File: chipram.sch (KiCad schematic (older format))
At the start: 26 parts, among them J500 Jumper_2_Bridged, U500 62402, U501 XX4256-15, U502 XX4256-15, U503 XX4256-15, U504 XX4256-15, U505 XX4256-15, U506 XX4256-15, U507 XX4256-15, U508 XX4256-15, U540 74F244, U541 74F244

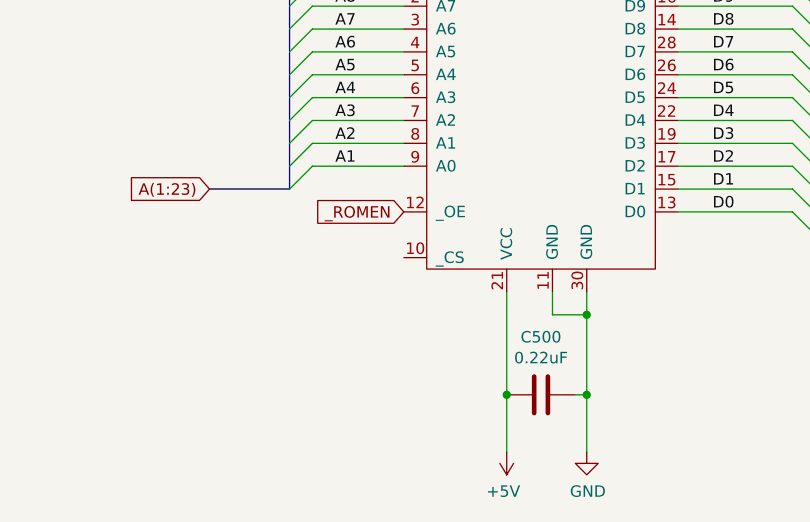
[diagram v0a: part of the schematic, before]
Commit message: Fix some DRC fuckery
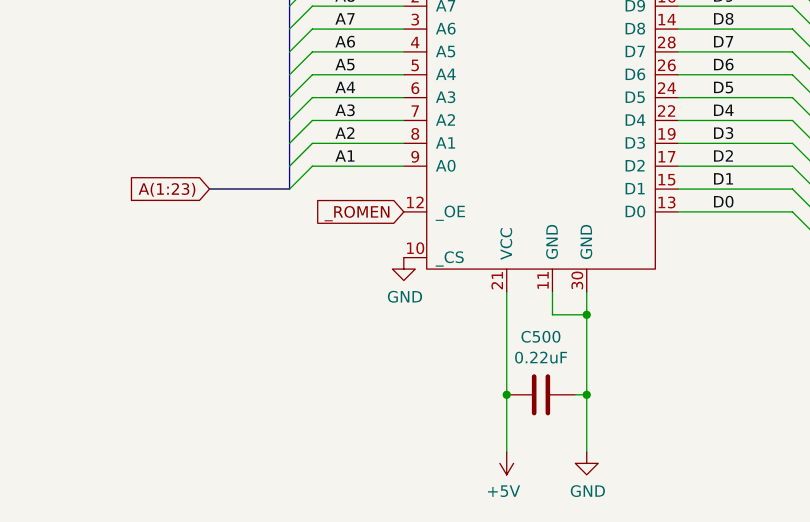
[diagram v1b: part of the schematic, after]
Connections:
- net GND: now also U500.10 (_CS)
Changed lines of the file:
@@
 Wire Bus Line
 	7350 9800 15750 9800
+$Comp
+L power:GND #PWR0257
+U 1 1 7152E7BF
+P 2500 10100
+F 0 "#PWR0257" H 2500 9850 50  0001 C CNN
+F 1 "GND" H 2505 9927 50  0000 C CNN
+F 2 "" H 2500 10100 50  0001 C CNN
+F 3 "" H 2500 10100 50  0001 C CNN
+	1    2500 10100
+	1    0    0    -1
+$EndComp
 $EndSCHEMATC

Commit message: drc
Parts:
- added C540, C541: 0.1uF, symbol Device:C
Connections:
- net +5V: now also U540.20 (VCC), U541.20 (VCC), C540.2, C541.2
- net GND: now also U540.1 (OEa), U540.10 (GND), U540.19 (OEb), U541.1 (OEa), U541.10 (GND), U541.19 (OEb), C540.1, C541.1
- net at RP502.1 (R1.1), U501.4 (_RAS), U502.4 (_RAS)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: no longer U505.4 (_RAS), U506.4 (_RAS), U507.4 (_RAS), U508.4 (_RAS)
- net at RP502.5 (R3.1): now also U505.4 (_RAS), U506.4 (_RAS), U507.4 (_RAS), U508.4 (_RAS)
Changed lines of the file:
@@
 	3650 3750 3650 5000
-Wire Wire Line
-	3650 5000 6300 5000
 Wire Wire Line
 	7200 5000 9700 5000
@@
 Connection ~ 12200 5000
 Wire Wire Line
-	6300 5000 6300 8000
-Wire Wire Line
-	6300 8000 7200 8000
-Connection ~ 6300 5000
-Wire Wire Line
-	6300 5000 7200 5000
-Wire Wire Line
 	7200 8000 9700 8000
-Connection ~ 7200 8000
 Wire Wire Line
 	9700 8000 12150 8000
@@
 Text GLabel 7350 9800 0    50   Input ~ 0
 DRD(0:15)
-Wire Bus Line
-	3750 1850 5850 1850
-Wire Bus Line
-	3750 3250 5850 3250
-Wire Bus Line
-	5850 1850 5850 3250
-Wire Bus Line
-	1250 1200 1250 3150
-Wire Bus Line
-	4300 8500 4300 10000
-Wire Bus Line
-	11750 3900 11750 9100
-Wire Bus Line
-	2000 8100 2000 9800
-Wire Bus Line
-	13800 3900 13800 9100
-Wire Bus Line
-	9300 3900 9300 9100
-Wire Bus Line
-	6800 3900 6800 9100
-Wire Bus Line
-	7650 6800 15750 6800
-Wire Bus Line
-	7350 9800 15750 9800
 $Comp
 L power:GND #PWR0257
@@
 	1    0    0    -1
 $EndComp
+Wire Wire Line
+	1600 2300 700  2300
+Wire Wire Line
+	700  2300 700  2400
+Wire Wire Line
+	700  2400 1600 2400
+Wire Wire Line
+	700  2400 700  2700
+Wire Wire Line
+	700  4150 1600 4150
+Connection ~ 700  2400
+Wire Wire Line
+	1600 4250 700  4250
+Wire Wire Line
+	700  4250 700  4150
+Connection ~ 700  4150
+$Comp
+L power:GND #PWR0258
+U 1 1 715AAAF3
+P 700 4650
+F 0 "#PWR0258" H 700 4400 50  0001 C CNN
+F 1 "GND" H 705 4477 50  0000 C CNN
+F 2 "" H 700 4650 50  0001 C CNN
+F 3 "" H 700 4650 50  0001 C CNN
+	1    700  4650
+	1    0    0    -1
+$EndComp
+Wire Wire Line
+	700  4250 700  4550
+Connection ~ 700  4250
+Wire Wire Line
+	2100 4550 700  4550
+Connection ~ 700  4550
+Wire Wire Line
+	700  4550 700  4650
+Wire Wire Line
+	2100 2700 700  2700
+Connection ~ 700  2700
+Wire Wire Line
+	700  2700 700  4150
+$Comp
+L Device:C C540
+U 1 1 716271D2
+P 2450 850
+F 0 "C540" H 2565 896 50  0000 L CNN
+F 1 "0.1uF" H 2565 805 50  0000 L CNN
+F 2 "" H 2488 700 50  0001 C CNN
+F 3 "~" H 2450 850 50  0001 C CNN
+	1    2450 850
+	1    0    0    -1
+$EndComp
+$Comp
+L Device:C C541
+U 1 1 71627735
+P 2500 2800
+F 0 "C541" H 2615 2846 50  0000 L CNN
+F 1 "0.1uF" H 2615 2755 50  0000 L CNN
+F 2 "" H 2538 2650 50  0001 C CNN
+F 3 "~" H 2500 2800 50  0001 C CNN
+	1    2500 2800
+	1    0    0    -1
+$EndComp
+Wire Wire Line
+	2250 2700 2250 2650
+Wire Wire Line
+	2250 2650 2500 2650
+Wire Wire Line
+	2100 2700 2250 2700
+Connection ~ 2100 2700
+Wire Wire Line
+	2500 2950 2100 2950
+$Comp
+L power:+5V #PWR0259
+U 1 1 716A9775
+P 1950 2900
+F 0 "#PWR0259" H 1950 2750 50  0001 C CNN
+F 1 "+5V" V 1965 3028 50  0000 L CNN
+F 2 "" H 1950 2900 50  0001 C CNN
+F 3 "" H 1950 2900 50  0001 C CNN
+	1    1950 2900
+	0    -1   -1   0
+$EndComp
+Connection ~ 2100 2950
+Wire Wire Line
+	1950 2900 2100 2900
+Wire Wire Line
+	2100 2900 2100 2950
+$Comp
+L power:+5V #PWR0260
+U 1 1 716D557D
+P 1950 1050
+F 0 "#PWR0260" H 1950 900 50  0001 C CNN
+F 1 "+5V" V 1965 1178 50  0000 L CNN
+F 2 "" H 1950 1050 50  0001 C CNN
+F 3 "" H 1950 1050 50  0001 C CNN
+	1    1950 1050
+	0    -1   -1   0
+$EndComp
+Wire Wire Line
+	1950 1050 2100 1050
+Wire Wire Line
+	2100 1050 2100 1100
+Wire Wire Line
+	2100 1050 2450 1050
+Wire Wire Line
+	2450 1050 2450 1000
+Connection ~ 2100 1050
+Wire Wire Line
+	700  700  2450 700
+Wire Wire Line
+	700  700  700  2300
+Connection ~ 700  2300
+Wire Wire Line
+	3650 5000 7200 5000
+Wire Wire Line
+	4250 8000 7200 8000
+Wire Wire Line
+	4250 3750 4250 8000
+Wire Bus Line
+	3750 1850 5850 1850
+Wire Bus Line
+	3750 3250 5850 3250
+Wire Bus Line
+	5850 1850 5850 3250
+Wire Bus Line
+	1250 1200 1250 3150
+Wire Bus Line
+	4300 8500 4300 10000
+Wire Bus Line
+	11750 3900 11750 9100
+Wire Bus Line
+	2000 8100 2000 9800
+Wire Bus Line
+	13800 3900 13800 9100
+Wire Bus Line
+	9300 3900 9300 9100
+Wire Bus Line
+	6800 3900 6800 9100
+Wire Bus Line
+	7650 6800 15750 6800
+Wire Bus Line
+	7350 9800 15750 9800
+Connection ~ 7200 8000
 $EndSCHEMATC

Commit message: Rename bus with correct syntax
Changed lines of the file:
@@
-EESchema Schematic File Version 4
+EESchema Schematic File Version 5
 LIBS:amiga2000-cache
 EELAYER 29 0
@@
 	4800 10000 4300 10000
 Text GLabel 1650 9800 0    50   Input ~ 0
-A(1:23)
+A[1..23]
 Text GLabel 4800 10000 2    50   Input ~ 0
-D(0:15)
+D[0..15]
 Text Label 2200 8000 0    50   ~ 0
 A18
@@
 	1250 2000 1350 2100
 Text GLabel 950  1200 0    50   Input ~ 0
-DRA(0:8)
+DRA[0..8]
 Wire Bus Line
 	950  1200 1250 1200
@@
 	15750 6800 15750 9800
 Text GLabel 7350 9800 0    50   Input ~ 0
-DRD(0:15)
+DRD[0..15]
 $Comp
 L power:GND #PWR0257
@@
 Wire Wire Line
 	4250 3750 4250 8000
+Connection ~ 7200 8000
 Wire Bus Line
 	3750 1850 5850 1850
@@
 Wire Bus Line
 	7350 9800 15750 9800
-Connection ~ 7200 8000
 $EndSCHEMATC

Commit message: Some ERC things
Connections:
- net +5V: now also C503.2, U503.10 (VCC); no longer C503.1, U503.20 (GND)
- net GND: now also C503.1, U503.20 (GND); no longer C503.2, U503.10 (VCC)
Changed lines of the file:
@@
-EESchema Schematic File Version 5
+EESchema Schematic File Version 4
 LIBS:amiga2000-cache
 EELAYER 29 0
@@
 L power:GND #PWR091
 U 1 1 5E8BEEE2
+P 13050 4300
+F 0 "#PWR091" H 13050 4050 50  0001 C CNN
+F 1 "GND" V 13055 4172 50  0000 R CNN
+F 2 "" H 13050 4300 50  0001 C CNN
+F 3 "" H 13050 4300 50  0001 C CNN
+	1    13050 4300
+	0    -1   -1   0
+$EndComp
+$Comp
+L power:+5V #PWR093
+U 1 1 5E8BEEE8
 P 12550 4300
-F 0 "#PWR091" H 12550 4050 50  0001 C CNN
-F 1 "GND" V 12555 4172 50  0000 R CNN
+F 0 "#PWR093" H 12550 4150 50  0001 C CNN
+F 1 "+5V" V 12565 4428 50  0000 L CNN
 F 2 "" H 12550 4300 50  0001 C CNN
 F 3 "" H 12550 4300 50  0001 C CNN
 	1    12550 4300
-	0    1    1    0
-$EndComp
-$Comp
-L power:+5V #PWR093
-U 1 1 5E8BEEE8
-P 13050 4300
-F 0 "#PWR093" H 13050 4150 50  0001 C CNN
-F 1 "+5V" V 13065 4428 50  0000 L CNN
-F 2 "" H 13050 4300 50  0001 C CNN
-F 3 "" H 13050 4300 50  0001 C CNN
-	1    13050 4300
-	0    1    1    0
-$EndComp
-Wire Wire Line
+	0    -1   -1   0
+$EndComp
+Wire Wire Line

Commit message: squeak
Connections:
- net +5V: now also C501.2, C502.2, C504.2, C505.2, C506.2, C507.2, C508.2, U501.10 (VCC), U502.10 (VCC), U504.10 (VCC), U505.10 (VCC), U506.10 (VCC), U507.10 (VCC), U508.10 (VCC); no longer C501.1, C502.1, C504.1, C505.1, C506.1, C507.1, C508.1, U501.20 (GND), U502.20 (GND), U504.20 (GND), U505.20 (GND), U506.20 (GND), U507.20 (GND), U508.20 (GND)
- net GND: now also C501.1, C502.1, C504.1, C505.1, C506.1, C507.1, C508.1, U501.20 (GND), U502.20 (GND), U504.20 (GND), U505.20 (GND), U506.20 (GND), U507.20 (GND), U508.20 (GND); no longer C501.2, C502.2, C504.2, C505.2, C506.2, C507.2, C508.2, U501.10 (VCC), U502.10 (VCC), U504.10 (VCC), U505.10 (VCC), U506.10 (VCC), U507.10 (VCC), U508.10 (VCC)
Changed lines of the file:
@@
 L power:GND #PWR078
 U 1 1 5E8B4169
+P 8050 4300
+F 0 "#PWR078" H 8050 4050 50  0001 C CNN
+F 1 "GND" V 8055 4172 50  0000 R CNN
+F 2 "" H 8050 4300 50  0001 C CNN
+F 3 "" H 8050 4300 50  0001 C CNN
+	1    8050 4300
+	0    -1   -1   0
+$EndComp
+$Comp
+L power:+5V #PWR080
+U 1 1 5E8B4981
 P 7550 4300
-F 0 "#PWR078" H 7550 4050 50  0001 C CNN
-F 1 "GND" V 7555 4172 50  0000 R CNN
+F 0 "#PWR080" H 7550 4150 50  0001 C CNN
+F 1 "+5V" V 7565 4428 50  0000 L CNN
 F 2 "" H 7550 4300 50  0001 C CNN
 F 3 "" H 7550 4300 50  0001 C CNN
 	1    7550 4300
-	0    1    1    0
-$EndComp
-$Comp
-L power:+5V #PWR080
-U 1 1 5E8B4981
-P 8050 4300
-F 0 "#PWR080" H 8050 4150 50  0001 C CNN
-F 1 "+5V" V 8065 4428 50  0000 L CNN
-F 2 "" H 8050 4300 50  0001 C CNN
-F 3 "" H 8050 4300 50  0001 C CNN
-	1    8050 4300
-	0    1    1    0
+	0    -1   -1   0
 $EndComp
 Wire Wire Line
@@
 L power:GND #PWR084
 U 1 1 5E8BAB5E
+P 10550 4300
+F 0 "#PWR084" H 10550 4050 50  0001 C CNN
+F 1 "GND" V 10555 4172 50  0000 R CNN
+F 2 "" H 10550 4300 50  0001 C CNN
+F 3 "" H 10550 4300 50  0001 C CNN
+	1    10550 4300
+	0    -1   -1   0
+$EndComp
+$Comp
+L power:+5V #PWR086
+U 1 1 5E8BAB68
 P 10050 4300
-F 0 "#PWR084" H 10050 4050 50  0001 C CNN
-F 1 "GND" V 10055 4172 50  0000 R CNN
+F 0 "#PWR086" H 10050 4150 50  0001 C CNN
+F 1 "+5V" V 10065 4428 50  0000 L CNN
 F 2 "" H 10050 4300 50  0001 C CNN
 F 3 "" H 10050 4300 50  0001 C CNN
 	1    10050 4300
-	0    1    1    0
-$EndComp
-$Comp
-L power:+5V #PWR086
-U 1 1 5E8BAB68
-P 10550 4300
-F 0 "#PWR086" H 10550 4150 50  0001 C CNN
-F 1 "+5V" V 10565 4428 50  0000 L CNN
-F 2 "" H 10550 4300 50  0001 C CNN
-F 3 "" H 10550 4300 50  0001 C CNN
-	1    10550 4300
-	0    1    1    0
+	0    -1   -1   0
 $EndComp
 Wire Wire Line
@@
 L power:GND #PWR096
 U 1 1 5E8C19D1
+P 15050 4300
+F 0 "#PWR096" H 15050 4050 50  0001 C CNN
+F 1 "GND" V 15055 4172 50  0000 R CNN
+F 2 "" H 15050 4300 50  0001 C CNN
+F 3 "" H 15050 4300 50  0001 C CNN
+	1    15050 4300
+	0    -1   -1   0
+$EndComp
+$Comp
+L power:+5V #PWR098
+U 1 1 5E8C19D7
 P 14550 4300
-F 0 "#PWR096" H 14550 4050 50  0001 C CNN
-F 1 "GND" V 14555 4172 50  0000 R CNN
+F 0 "#PWR098" H 14550 4150 50  0001 C CNN
+F 1 "+5V" V 14565 4428 50  0000 L CNN
 F 2 "" H 14550 4300 50  0001 C CNN
 F 3 "" H 14550 4300 50  0001 C CNN
 	1    14550 4300
-	0    1    1    0
-$EndComp
-$Comp
-L power:+5V #PWR098
-U 1 1 5E8C19D7
-P 15050 4300
-F 0 "#PWR098" H 15050 4150 50  0001 C CNN
-F 1 "+5V" V 15065 4428 50  0000 L CNN
-F 2 "" H 15050 4300 50  0001 C CNN
-F 3 "" H 15050 4300 50  0001 C CNN
-	1    15050 4300
-	0    1    1    0
+	0    -1   -1   0
 $EndComp
 Wire Wire Line
@@
 L power:GND #PWR097
 U 1 1 5E8C4677
+P 15050 7300
+F 0 "#PWR097" H 15050 7050 50  0001 C CNN
+F 1 "GND" V 15055 7172 50  0000 R CNN
+F 2 "" H 15050 7300 50  0001 C CNN
+F 3 "" H 15050 7300 50  0001 C CNN
+	1    15050 7300
+	0    -1   -1   0
+$EndComp
+$Comp
+L power:+5V #PWR099
+U 1 1 5E8C467D
 P 14550 7300
-F 0 "#PWR097" H 14550 7050 50  0001 C CNN
-F 1 "GND" V 14555 7172 50  0000 R CNN
+F 0 "#PWR099" H 14550 7150 50  0001 C CNN
+F 1 "+5V" V 14565 7428 50  0000 L CNN
 F 2 "" H 14550 7300 50  0001 C CNN
 F 3 "" H 14550 7300 50  0001 C CNN
 	1    14550 7300
-	0    1    1    0
-$EndComp
-$Comp
-L power:+5V #PWR099
-U 1 1 5E8C467D
-P 15050 7300
-F 0 "#PWR099" H 15050 7150 50  0001 C CNN
-F 1 "+5V" V 15065 7428 50  0000 L CNN
-F 2 "" H 15050 7300 50  0001 C CNN
-F 3 "" H 15050 7300 50  0001 C CNN
-	1    15050 7300
-	0    1    1    0
+	0    -1   -1   0
 $EndComp
 Wire Wire Line
@@
 L power:GND #PWR090
 U 1 1 5E8CAD29
+P 13000 7300
+F 0 "#PWR090" H 13000 7050 50  0001 C CNN
+F 1 "GND" V 13005 7172 50  0000 R CNN
+F 2 "" H 13000 7300 50  0001 C CNN
+F 3 "" H 13000 7300 50  0001 C CNN
+	1    13000 7300
+	0    -1   -1   0
+$EndComp
+$Comp
+L power:+5V #PWR092
+U 1 1 5E8CAD2F
 P 12500 7300
-F 0 "#PWR090" H 12500 7050 50  0001 C CNN
-F 1 "GND" V 12505 7172 50  0000 R CNN
+F 0 "#PWR092" H 12500 7150 50  0001 C CNN
+F 1 "+5V" V 12515 7428 50  0000 L CNN
 F 2 "" H 12500 7300 50  0001 C CNN
 F 3 "" H 12500 7300 50  0001 C CNN
 	1    12500 7300
-	0    1    1    0
-$EndComp
-$Comp
-L power:+5V #PWR092
-U 1 1 5E8CAD2F
-P 13000 7300
-F 0 "#PWR092" H 13000 7150 50  0001 C CNN
-F 1 "+5V" V 13015 7428 50  0000 L CNN
-F 2 "" H 13000 7300 50  0001 C CNN
-F 3 "" H 13000 7300 50  0001 C CNN
-	1    13000 7300
-	0    1    1    0
-$EndComp
-Wire Wire Line
-	13000 7300 12950 7300
-Wire Wire Line
-	12500 7300 12550 7300
-Wire Wire Line
-	12550 7300 12550 7450
-Wire Wire Line
-	12700 7450 12700 7600
-Wire Wire Line
-	12550 7450 12700 7450
-Connection ~ 12550 7300
-Wire Wire Line
-	12550 7300 12600 7300
-Wire Wire Line
-	12800 7450 12950 7450
-Wire Wire Line
-	12950 7450 12950 7300
-Connection ~ 12950 7300
-Wire Wire Line
-	12950 7300 12900 7300
+	0    -1   -1   0
+$EndComp
 Wire Wire Line
 	12800 7450 12800 7600
@@
 L power:GND #PWR085
 U 1 1 5E8D123B
+P 10550 7300
+F 0 "#PWR085" H 10550 7050 50  0001 C CNN
+F 1 "GND" V 10555 7172 50  0000 R CNN
+F 2 "" H 10550 7300 50  0001 C CNN
+F 3 "" H 10550 7300 50  0001 C CNN
+	1    10550 7300
+	0    -1   -1   0
+$EndComp
+$Comp
+L power:+5V #PWR087
+U 1 1 5E8D1241
 P 10050 7300
-F 0 "#PWR085" H 10050 7050 50  0001 C CNN
-F 1 "GND" V 10055 7172 50  0000 R CNN
+F 0 "#PWR087" H 10050 7150 50  0001 C CNN
+F 1 "+5V" V 10065 7428 50  0000 L CNN
 F 2 "" H 10050 7300 50  0001 C CNN
 F 3 "" H 10050 7300 50  0001 C CNN
 	1    10050 7300
-	0    1    1    0
-$EndComp
-$Comp
-L power:+5V #PWR087
-U 1 1 5E8D1241
-P 10550 7300
-F 0 "#PWR087" H 10550 7150 50  0001 C CNN
-F 1 "+5V" V 10565 7428 50  0000 L CNN
-F 2 "" H 10550 7300 50  0001 C CNN
-F 3 "" H 10550 7300 50  0001 C CNN
-	1    10550 7300
-	0    1    1    0
+	0    -1   -1   0
 $EndComp
 Wire Wire Line
@@
 L power:GND #PWR079
 U 1 1 5E8D49C4
+P 8050 7300
+F 0 "#PWR079" H 8050 7050 50  0001 C CNN
+F 1 "GND" V 8055 7172 50  0000 R CNN
+F 2 "" H 8050 7300 50  0001 C CNN
+F 3 "" H 8050 7300 50  0001 C CNN
+	1    8050 7300
+	0    -1   -1   0
+$EndComp
+$Comp
+L power:+5V #PWR081
+U 1 1 5E8D49CA
 P 7550 7300
-F 0 "#PWR079" H 7550 7050 50  0001 C CNN
-F 1 "GND" V 7555 7172 50  0000 R CNN
+F 0 "#PWR081" H 7550 7150 50  0001 C CNN
+F 1 "+5V" V 7565 7428 50  0000 L CNN
 F 2 "" H 7550 7300 50  0001 C CNN
 F 3 "" H 7550 7300 50  0001 C CNN
 	1    7550 7300
-	0    1    1    0
-$EndComp
-$Comp
-L power:+5V #PWR081
-U 1 1 5E8D49CA
-P 8050 7300
-F 0 "#PWR081" H 8050 7150 50  0001 C CNN
-F 1 "+5V" V 8065 7428 50  0000 L CNN
-F 2 "" H 8050 7300 50  0001 C CNN
-F 3 "" H 8050 7300 50  0001 C CNN
-	1    8050 7300
-	0    1    1    0
+	0    -1   -1   0
 $EndComp
 Wire Wire Line
@@
 L power:GND #PWR0257
 U 1 1 7152E7BF
-P 2500 10100
-F 0 "#PWR0257" H 2500 9850 50  0001 C CNN
-F 1 "GND" H 2505 9927 50  0000 C CNN
-F 2 "" H 2500 10100 50  0001 C CNN
-F 3 "" H 2500 10100 50  0001 C CNN
-	1    2500 10100
+P 2400 10250
+F 0 "#PWR0257" H 2400 10000 50  0001 C CNN
+F 1 "GND" H 2405 10077 50  0000 C CNN
+F 2 "" H 2400 10250 50  0001 C CNN
+F 3 "" H 2400 10250 50  0001 C CNN
+	1    2400 10250
 	1    0    0    -1
 $EndComp
@@
 	4250 3750 4250 8000
 Connection ~ 7200 8000
+Wire Wire Line
+	2400 10250 2400 10100
+Wire Wire Line
+	2400 10100 2500 10100
+Wire Wire Line
+	12800 7450 12950 7450
+Wire Wire Line
+	12950 7450 12950 7300
+Wire Wire Line
+	12950 7300 12900 7300
+Wire Wire Line
+	12950 7300 13000 7300
+Connection ~ 12950 7300
+Wire Wire Line
+	12700 7600 12700 7450
+Wire Wire Line
+	12700 7450 12550 7450
+Wire Wire Line
+	12550 7450 12550 7300
+Wire Wire Line
+	12550 7300 12600 7300
+Wire Wire Line
+	12550 7300 12500 7300
 Wire Bus Line
 	3750 1850 5850 1850
@@
 Wire Bus Line
 	7350 9800 15750 9800
+Connection ~ 12550 7300
 $EndSCHEMATC

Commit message: Associate footprints with components
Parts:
- J500: footprint (none) -> Connector_PinSocket_2.54mm:PinSocket_2x01_P2.54mm_Vertical
- R500: footprint (none) -> Resistor_THT:R_Axial_DIN0207_L6.3mm_D2.5mm_P10.16mm_Horizontal
- U500: footprint (none) -> Package_DIP:DIP-40_W15.24mm_Socket
- U501, U502, U503, U504, U505, U506, U507, U508, U540, U541: footprint (none) -> Package_DIP:DIP-20_W7.62mm_Socket
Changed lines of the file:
@@
 F 0 "U540" H 2250 2600 50  0000 C CNN
 F 1 "74F244" H 1850 2600 50  0000 C CNN
-F 2 "" H 2100 1900 50  0001 C CNN
+F 2 "Package_DIP:DIP-20_W7.62mm_Socket" H 2100 1900 50  0001 C CNN
 F 3 "http://www.ti.com/lit/gpn/sn74LS244" H 2100 1900 50  0001 C CNN
 	1    2100 1900
@@
 F 0 "U541" H 2250 4450 50  0000 C CNN
 F 1 "74F244" H 1850 4450 50  0000 C CNN
-F 2 "" H 2100 3750 50  0001 C CNN
+F 2 "Package_DIP:DIP-20_W7.62mm_Socket" H 2100 3750 50  0001 C CNN
 F 3 "http://www.ti.com/lit/gpn/sn74LS244" H 2100 3750 50  0001 C CNN
 	1    2100 3750
@@
 F 0 "U500" H 3100 8025 50  0000 C CNN
 F 1 "62402" H 3100 7934 50  0000 C CNN
-F 2 "" H 3100 7900 50  0001 C CNN
+F 2 "Package_DIP:DIP-40_W15.24mm_Socket" H 3100 7900 50  0001 C CNN
 F 3 "" H 3100 7900 50  0001 C CNN
 	1    3100 7900
@@
 F 0 "R500" H 1370 7296 50  0000 L CNN
 F 1 "4.7k" H 1370 7205 50  0000 L CNN
-F 2 "" V 1230 7250 50  0001 C CNN
+F 2 "Resistor_THT:R_Axial_DIN0207_L6.3mm_D2.5mm_P10.16mm_Horizontal" V 1230 7250 50  0001 C CNN
 F 3 "~" H 1300 7250 50  0001 C CNN
 	1    1300 7250
@@
 F 0 "J500" H 1750 7603 50  0000 C CNN
 F 1 "Jumper_2_Bridged" H 1750 7604 50  0001 C CNN
-F 2 "" H 1750 7500 50  0001 C CNN
+F 2 "Connector_PinSocket_2.54mm:PinSocket_2x01_P2.54mm_Vertical" H 1750 7500 50  0001 C CNN
 F 3 "~" H 1750 7500 50  0001 C CNN
 	1    1750 7500
@@
 F 0 "U501" H 8078 3971 50  0000 L CNN
 F 1 "XX4256-15" H 8078 3880 50  0000 L CNN
-F 2 "" H 7700 4700 50  0001 C CNN
+F 2 "Package_DIP:DIP-20_W7.62mm_Socket" H 7700 4700 50  0001 C CNN
 F 3 "" H 7700 4700 50  0001 C CNN
 	1    7700 4700
@@
 F 0 "U505" H 8078 6971 50  0000 L CNN
 F 1 "XX4256-15" H 8078 6880 50  0000 L CNN
-F 2 "" H 7700 7700 50  0001 C CNN
+F 2 "Package_DIP:DIP-20_W7.62mm_Socket" H 7700 7700 50  0001 C CNN
 F 3 "" H 7700 7700 50  0001 C CNN
 	1    7700 7700
@@
 F 0 "U506" H 10578 6971 50  0000 L CNN
 F 1 "XX4256-15" H 10578 6880 50  0000 L CNN
-F 2 "" H 10200 7700 50  0001 C CNN
+F 2 "Package_DIP:DIP-20_W7.62mm_Socket" H 10200 7700 50  0001 C CNN
 F 3 "" H 10200 7700 50  0001 C CNN
 	1    10200 7700
@@
 F 0 "U507" H 13028 6971 50  0000 L CNN
 F 1 "XX4256-15" H 13028 6880 50  0000 L CNN
-F 2 "" H 12650 7700 50  0001 C CNN
+F 2 "Package_DIP:DIP-20_W7.62mm_Socket" H 12650 7700 50  0001 C CNN
 F 3 "" H 12650 7700 50  0001 C CNN
 	1    12650 7700
@@
 F 0 "U508" H 15078 6971 50  0000 L CNN
 F 1 "XX4256-15" H 15078 6880 50  0000 L CNN
-F 2 "" H 14700 7700 50  0001 C CNN
+F 2 "Package_DIP:DIP-20_W7.62mm_Socket" H 14700 7700 50  0001 C CNN
 F 3 "" H 14700 7700 50  0001 C CNN
 	1    14700 7700
@@
 F 0 "U502" H 10578 3971 50  0000 L CNN
 F 1 "XX4256-15" H 10578 3880 50  0000 L CNN
-F 2 "" H 10200 4700 50  0001 C CNN
+F 2 "Package_DIP:DIP-20_W7.62mm_Socket" H 10200 4700 50  0001 C CNN
 F 3 "" H 10200 4700 50  0001 C CNN
 	1    10200 4700
@@
 F 0 "U503" H 13078 3971 50  0000 L CNN
 F 1 "XX4256-15" H 13078 3880 50  0000 L CNN
-F 2 "" H 12700 4700 50  0001 C CNN
+F 2 "Package_DIP:DIP-20_W7.62mm_Socket" H 12700 4700 50  0001 C CNN
 F 3 "" H 12700 4700 50  0001 C CNN
 	1    12700 4700
@@
 F 0 "U504" H 15078 3971 50  0000 L CNN
 F 1 "XX4256-15" H 15078 3880 50  0000 L CNN
-F 2 "" H 14700 4700 50  0001 C CNN
+F 2 "Package_DIP:DIP-20_W7.62mm_Socket" H 14700 4700 50  0001 C CNN
 F 3 "" H 14700 4700 50  0001 C CNN
 	1    14700 4700
